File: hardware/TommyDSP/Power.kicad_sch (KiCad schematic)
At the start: 29 parts, among them J401 Conn_01x02_Pin, Q401 AO3401A, U401 TPS7A2033PDBVR, U402 TPS62A01APDDC, U403 TP4056-42-ESOP8

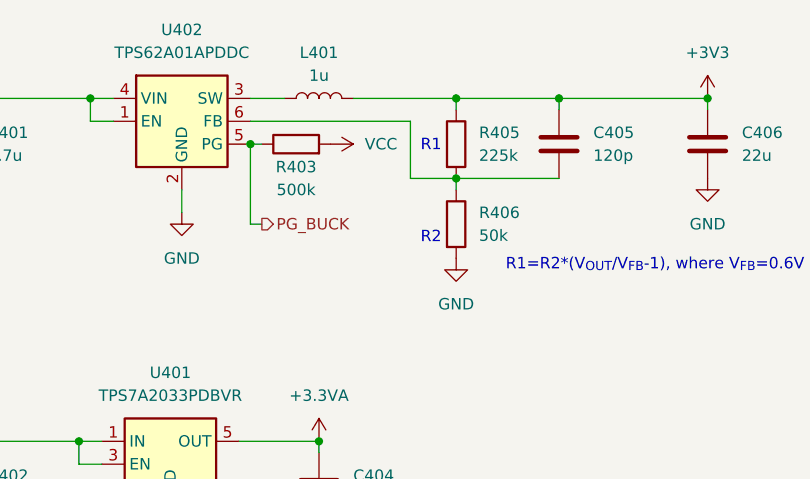
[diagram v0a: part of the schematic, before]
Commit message: hardware: adjust value of BUCK feedback resistors
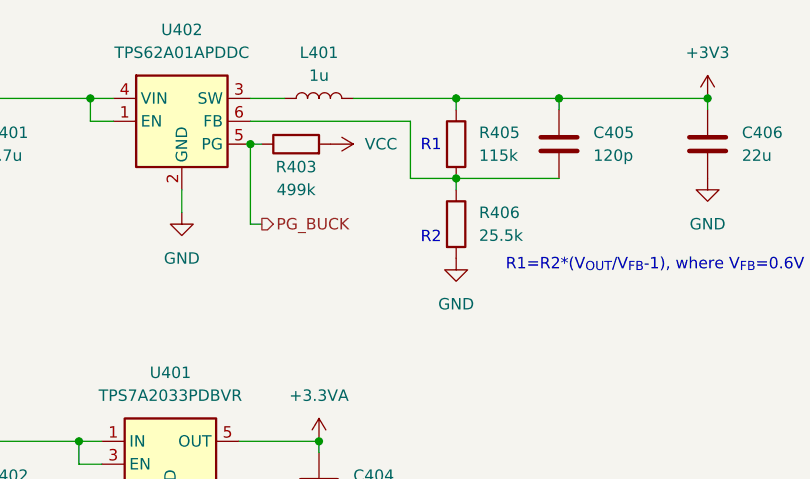
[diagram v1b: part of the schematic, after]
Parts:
- R403: value 500k -> 499k
- R405: value 225k -> 115k
- R406: value 50k -> 25.5k
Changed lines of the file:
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@@
 			)
 		)
-		(property "Value" "500k"
+		(property "Value" "499k"
 			(at 88.9 60.96 90)
 			(effects
@@
 			)
 		)
-		(property "Value" "50k"
+		(property "Value" "25.5k"
 			(at 109.22 66.0399 0)
 			(effects
@@
 			)
 		)
-		(property "Value" "225k"
+		(property "Value" "115k"
 			(at 109.22 57.1499 0)
 			(effects
